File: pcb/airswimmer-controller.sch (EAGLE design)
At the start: 49 parts, among them M1+ SOLDER_PAD.05X.05, M1- SOLDER_PAD.05X.05, M2+ SOLDER_PAD.05X.05, M2- SOLDER_PAD.05X.05, Q1 MOSFET-NCHANNELBSS123LT1G, Q2 MOSFET-NCHANNELBSS123LT1G, Y1 16MHz

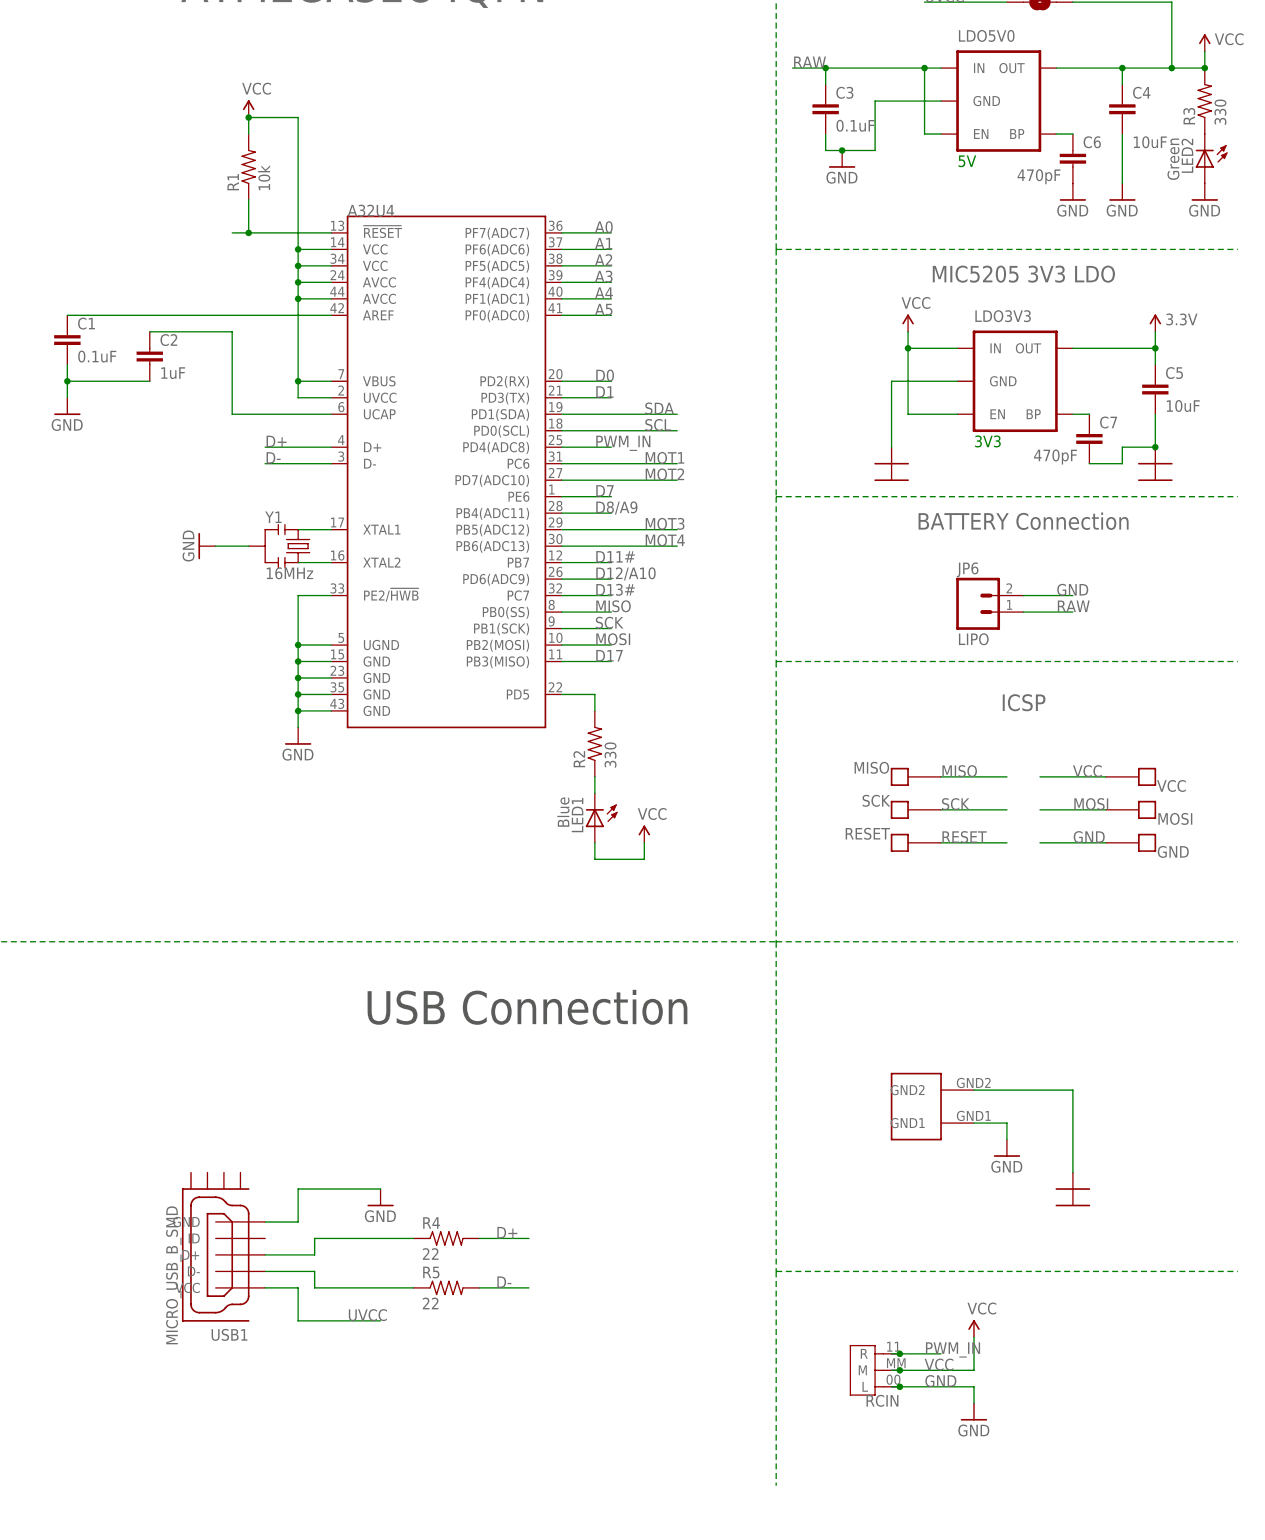
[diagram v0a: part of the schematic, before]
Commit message: Correct LED cathode direction in schematic and board.
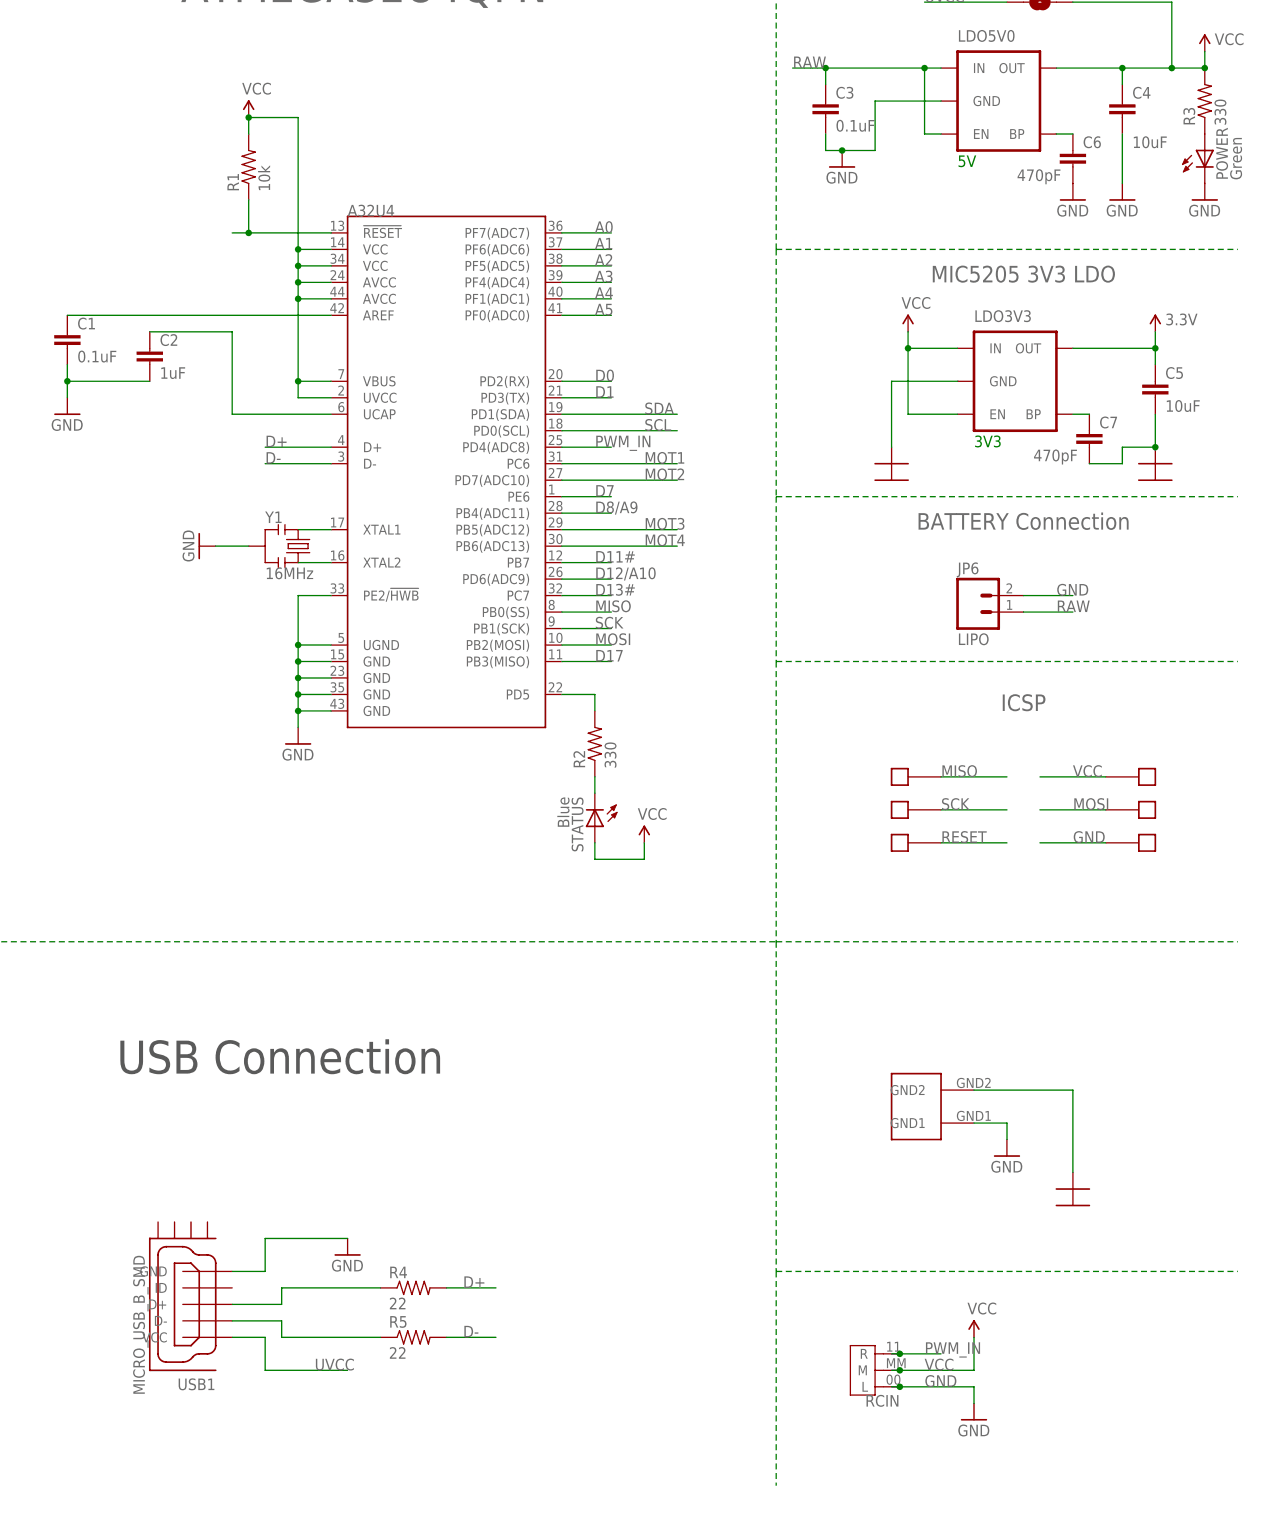
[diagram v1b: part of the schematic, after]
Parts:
- removed LED2: Green, SparkFun-LED:LED0603
- added POWER: Green, SparkFun-LED:LED0603
- renumbered LED1 to STATUS
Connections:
- net GND: now also POWER.C; no longer LED2.A
- net N$10: now also POWER.A; no longer LED2.C
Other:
- moved on the sheet: R4, R5, USB1
